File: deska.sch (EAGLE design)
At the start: 14 parts, among them X1 JST-XH-03-PIN-LONG-PAD

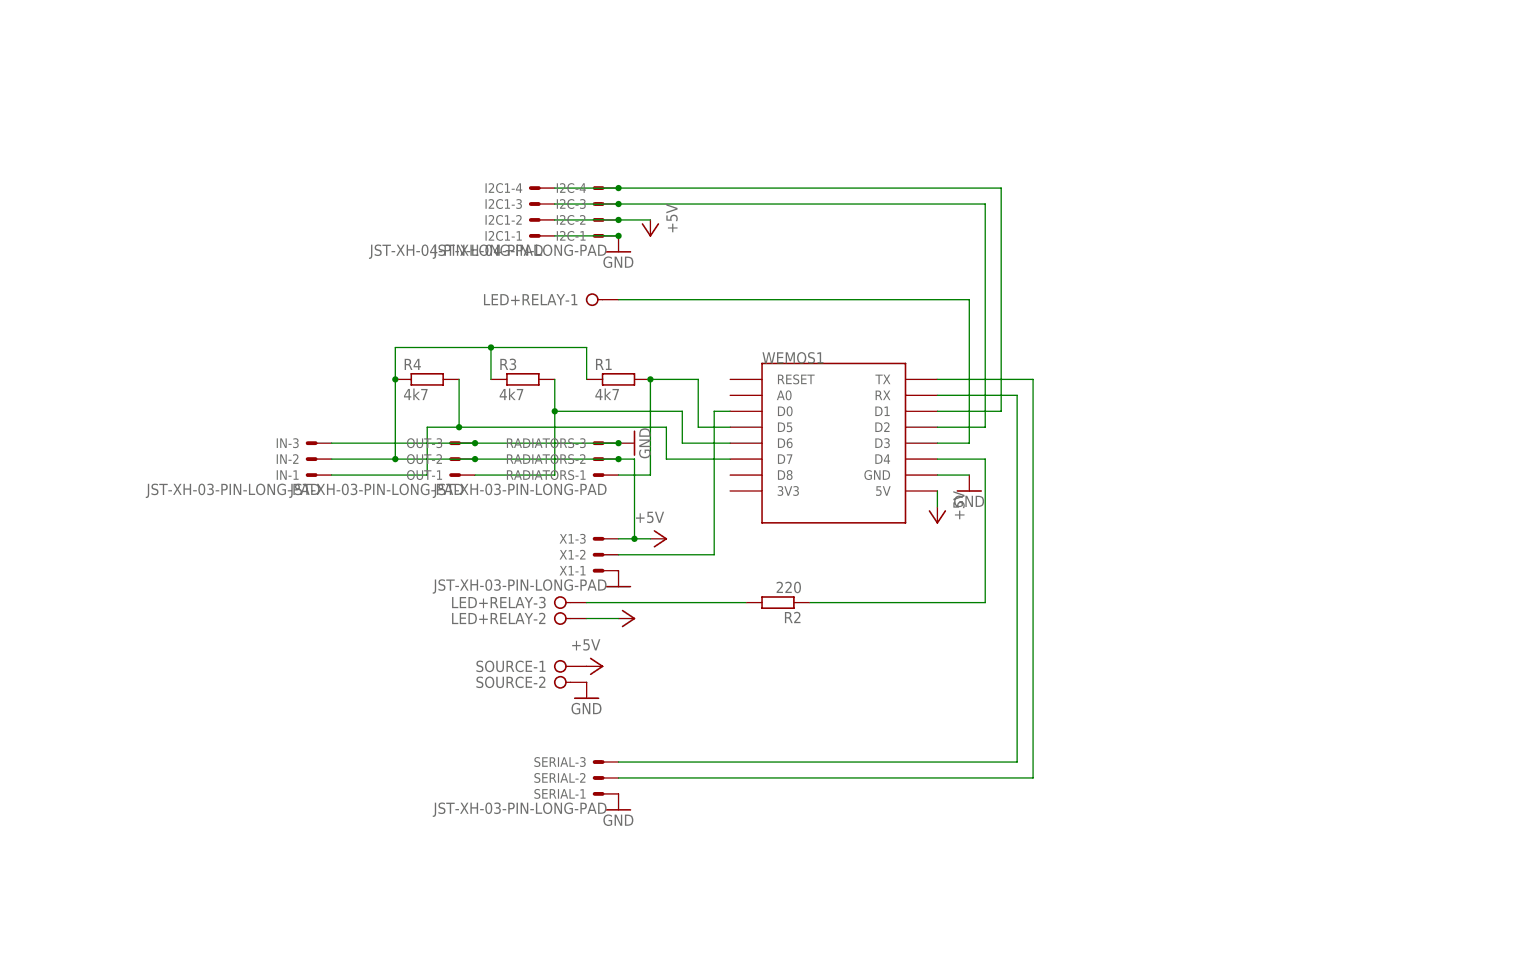
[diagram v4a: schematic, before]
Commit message: pridana ledka konektory
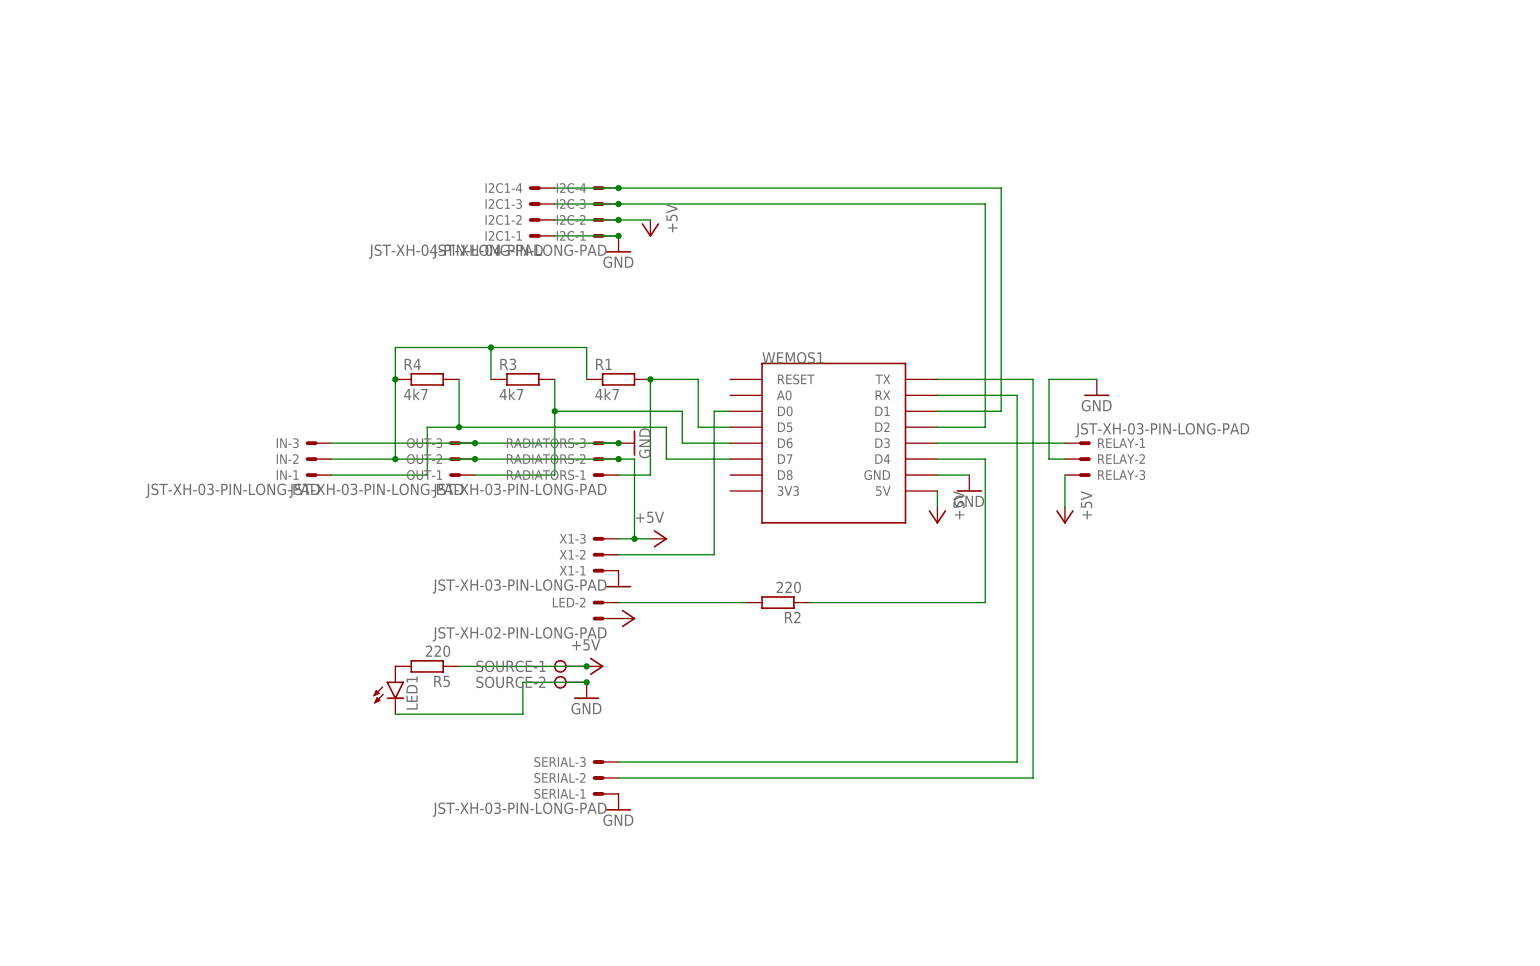
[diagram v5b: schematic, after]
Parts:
- removed LED+RELAY: (no value), con-wago-508:W237-03P
- added LED: JST-XH-02-PIN-LONG-PAD, Rembrandt Electronics - JST XH Connectors v1-0:JST-XH-02-PIN-LONG-PAD
- added LED1: (no value), led:LED3MM
- added R5: 220, rcl:R-EU_0207/10
- added RELAY: JST-XH-03-PIN-LONG-PAD, Rembrandt Electronics - JST XH Connectors v1-0:JST-XH-03-PIN-LONG-PAD
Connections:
- new net N$10: LED1.A, R5.2
- net +5V: now also LED-1.S, R5.1, RELAY-3.S; no longer LED+RELAY-2.KL
- net GND: now also LED1.C, RELAY-2.S
- net N$7: now also RELAY-1.S; no longer LED+RELAY-1.KL
- net N$8: now also LED-2.S; no longer LED+RELAY-3.KL

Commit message: +
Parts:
- removed I2C, I2C1: JST-XH-04-PIN-LONG-PAD, Rembrandt Electronics - JST XH Connectors v1-0:JST-XH-04-PIN-LONG-PAD
- removed IN, OUT, RADIATORS, SERIAL, X1: JST-XH-03-PIN-LONG-PAD, Rembrandt Electronics - JST XH Connectors v1-0:JST-XH-03-PIN-LONG-PAD
- removed SOURCE: (no value), con-wago-508:W237-02P
- added BUZZER, NAPAJENI: (no value), con-wago-508:W237-02P
- added I2CDISP, I2CKEYB: (no value), con-wago-508:W237-04P
- added Q1: BC547, transistor-npn:BC547
- added R6: 1k, rcl:R-EU_0207/7
- added TIN, TOUT, TUT: (no value), con-wago-508:W237-3E
- LED: value JST-XH-02-PIN-LONG-PAD -> (none); device Rembrandt Electronics - JST XH Connectors v1-0:JST-XH-02-PIN-LONG-PAD -> con-wago-508:W237-02P
- LED1: device led:LED3MM -> con-wago-508:W237-02P
- R1, R3, R5: device rcl:R-EU_0207/10 -> rcl:R-EU_0207/7
- R2: value 220 -> 4k7; device rcl:R-EU_0207/10 -> rcl:R-EU_0207/7
- R4: value 4k7 -> 220; device rcl:R-EU_0207/10 -> rcl:R-EU_0207/7
- RELAY: value JST-XH-03-PIN-LONG-PAD -> (none); device Rembrandt Electronics - JST XH Connectors v1-0:JST-XH-03-PIN-LONG-PAD -> con-wago-508:W237-02P
- WEMOS1: device esp8266modules:WEMOS-D1-MINI -> wemos:WEMOS-D1-MINI
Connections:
- removed net N$10: LED1.A, R5.2
- removed net N$13: OUT-1.S, R3.2, WEMOS1.D6
- removed net N$4: I2C-3.S, I2C1-3.S, WEMOS1.D2
- removed net N$9: IN-1.S, R4.2, WEMOS1.D7
- new net N$12: I2CDISP-3.KL, I2CKEYB-3.KL, WEMOS1.D2
- new net N$14: R5.1, RELAY-1.KL, WEMOS1.D3
- new net N$15: BUZZER-1.KL, Q1.C
- new net N$19: R2.1, TOUT-3.KL, WEMOS1.D5
- net +5V: now also I2CDISP-2.KL, I2CKEYB-2.KL, LED-2.KL, LED1-1.KL, NAPAJENI-1.KL, R1.2, R2.2, R3.2, RELAY-2.KL, TIN-2.KL, TOUT-2.KL, TUT-2.KL; no longer I2C-2.S, I2C1-2.S, IN-2.S, LED-1.S, OUT-2.S, R1.1, R3.1, R4.1, R5.1, RADIATORS-2.S, RELAY-3.S, SOURCE-1.KL, X1-3.S
- net GND: now also BUZZER-2.KL, I2CDISP-1.KL, I2CKEYB-1.KL, NAPAJENI-2.KL, Q1.E, TIN-1.KL, TOUT-1.KL, TUT-1.KL; no longer I2C-1.S, I2C1-1.S, IN-3.S, LED1.C, OUT-3.S, RADIATORS-3.S, RELAY-2.S, SERIAL-1.S, SOURCE-2.KL, X1-1.S
- net N$1: now also R1.1, TIN-3.KL, WEMOS1.D0; no longer SERIAL-2.S, WEMOS1.TX
- net N$11: now also I2CDISP-4.KL, I2CKEYB-4.KL, WEMOS1.D1; no longer R1.2, RADIATORS-1.S, WEMOS1.D5
- net N$2: now also LED1-2.KL, R5.2; no longer SERIAL-3.S, WEMOS1.RX
- net N$3: now also R3.1, TUT-3.KL, WEMOS1.D6; no longer I2C-4.S, I2C1-4.S, WEMOS1.D1
- net N$5: now also R4.1, WEMOS1.D8; no longer WEMOS1.D0, X1-2.S
- net N$6: now also LED-1.KL, R4.2; no longer R2.1, WEMOS1.D4
- net N$7: now also Q1.B, R6.1; no longer RELAY-1.S, WEMOS1.D3
- net N$8: now also R6.2, WEMOS1.D7; no longer LED-2.S, R2.2
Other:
- moved on the sheet: R1, R2, R3, R4, R5, WEMOS1

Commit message: +
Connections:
- new net BUILTINLED: WEMOS1.D4
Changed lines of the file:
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@@
+</segment>
+</net>
+<net name="BUILTINLED" class="0">
+<segment>
+<pinref part="WEMOS1" gate="D1" pin="D4"/>
+<wire x1="81.28" y1="58.42" x2="86.36" y2="58.42" width="0.1524" layer="91"/>
+<label x="86.36" y="58.42" size="1.778" layer="95"/>
 </segment>
 </net>

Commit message: upravy kodu
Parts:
- removed I2CDISP, I2CKEYB: (no value), con-wago-508:W237-04P
- removed LED: (no value), con-wago-508:W237-02P
- removed TIN, TOUT, TUT: (no value), con-wago-508:W237-3E
- added LEDRELAY: JST-XH-02-PIN-LONG-PAD, Rembrandt Electronics - JST XH Connectors v1-0:JST-XH-02-PIN-LONG-PAD
- added X1, X2, X3: JST-XH-03-PIN-LONG-PAD, Rembrandt Electronics - JST XH Connectors v1-0:JST-XH-03-PIN-LONG-PAD
- added X4, X5, X6: JST-XH-04-PIN-LONG-PAD, Rembrandt Electronics - JST XH Connectors v1-0:JST-XH-04-PIN-LONG-PAD
- BUZZER, LED1: value (none) -> JST-XH-02-PIN-LONG-PAD; device con-wago-508:W237-02P -> Rembrandt Electronics - JST XH Connectors v1-0:JST-XH-02-PIN-LONG-PAD
- RELAY: value (none) -> JST-XH-03-PIN-LONG-PAD; device con-wago-508:W237-02P -> Rembrandt Electronics - JST XH Connectors v1-0:JST-XH-03-PIN-LONG-PAD
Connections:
- new net +3V3: LED1-2.S, LEDRELAY-2.S, R1.2, R2.2, R3.2, WEMOS1.3V3, X1-2.S, X2-2.S, X3-2.S
- new net N$9: WEMOS1.GND, X4-3.S, X5-3.S, X6-3.S
- net +5V: now also BUZZER-1.S, RELAY-2.S, X4-4.S, X5-4.S, X6-4.S; no longer I2CDISP-2.KL, I2CKEYB-2.KL, LED-2.KL, LED1-1.KL, R1.2, R2.2, R3.2, RELAY-2.KL, TIN-2.KL, TOUT-2.KL, TUT-2.KL
- net GND: now also RELAY-3.S, X1-3.S, X2-3.S, X3-3.S; no longer BUZZER-2.KL, I2CDISP-1.KL, I2CKEYB-1.KL, TIN-1.KL, TOUT-1.KL, TUT-1.KL, WEMOS1.GND
- net N$1: now also X1-1.S; no longer TIN-3.KL
- net N$11: now also X4-1.S, X5-1.S, X6-1.S; no longer I2CDISP-4.KL, I2CKEYB-4.KL
- net N$12: now also X4-2.S, X5-2.S, X6-2.S; no longer I2CDISP-3.KL, I2CKEYB-3.KL
- net N$14: now also RELAY-1.S; no longer RELAY-1.KL
- net N$15: now also BUZZER-2.S; no longer BUZZER-1.KL
- net N$19: now also X2-1.S; no longer TOUT-3.KL
- net N$2: now also LEDRELAY-1.S; no longer LED1-2.KL
- net N$3: now also X3-1.S; no longer TUT-3.KL
- net N$6: now also LED1-1.S; no longer LED-1.KL
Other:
- moved on the sheet: NAPAJENI-1, NAPAJENI-2, R6
